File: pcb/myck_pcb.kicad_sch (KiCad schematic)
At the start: 42 parts, among them SW1 SW_Push, SW10 SW_Push, SW11 SW_Push, SW12 SW_Push, SW13 SW_Push, SW14 SW_Push, SW15 SW_Push, SW16 SW_Push, SW17 SW_Push, SW18 SW_Push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

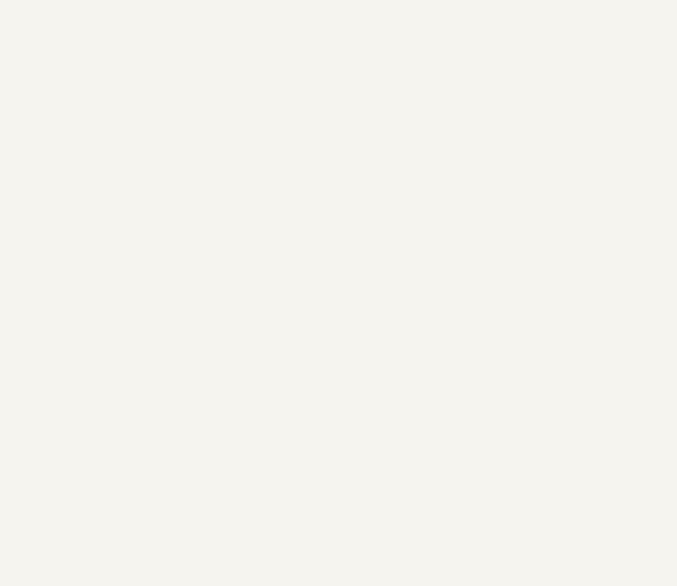
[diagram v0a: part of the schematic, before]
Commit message: Añadidos footprints propios y empezando la PCB
Añadidos footprints propios para:
- diodos
- switches
- microcontrolador
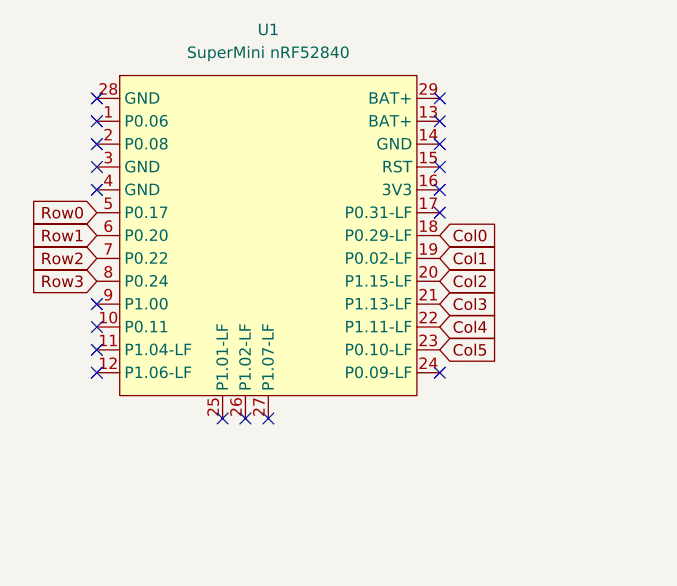
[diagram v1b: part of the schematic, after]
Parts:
- added U1: SuperMini nRF52840, myck:SuperMini_nRF52840_AH_USBup, symbol PCM_marbastlib-promicroish:SuperMini_nRF52840
- D1, D10, D11, D12, D13, D14, D15, D16, D17, D18, D19, D2, D20, D21, D3, D4, D5, D6, D7, D8, D9: footprint (none) -> myck:Diode_TH_SMD_DUAL
- SW1, SW10, SW11, SW12, SW13, SW14, SW15, SW16, SW17, SW18, SW19, SW2, SW20, SW21, SW3, SW4, SW5, SW6, SW7, SW8, SW9: footprint (none) -> myck:KS-27_KS-33_Hotswap_1U_DUAL
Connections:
- net Col0: now also U1.18 (P0.29-LF)
- net Col1: now also U1.19 (P0.02-LF)
- net Col2: now also U1.20 (P1.15-LF)
- net Col3: now also U1.21 (P1.13-LF)
- net Col4: now also U1.22 (P1.11-LF)
- net Col5: now also U1.23 (P0.10-LF)
- net Row0: now also U1.5 (P0.17)
- net Row1: now also U1.6 (P0.20)
- net Row2: now also U1.7 (P0.22)
- net Row3: now also U1.8 (P0.24)
- no-connect marks 0 -> 19

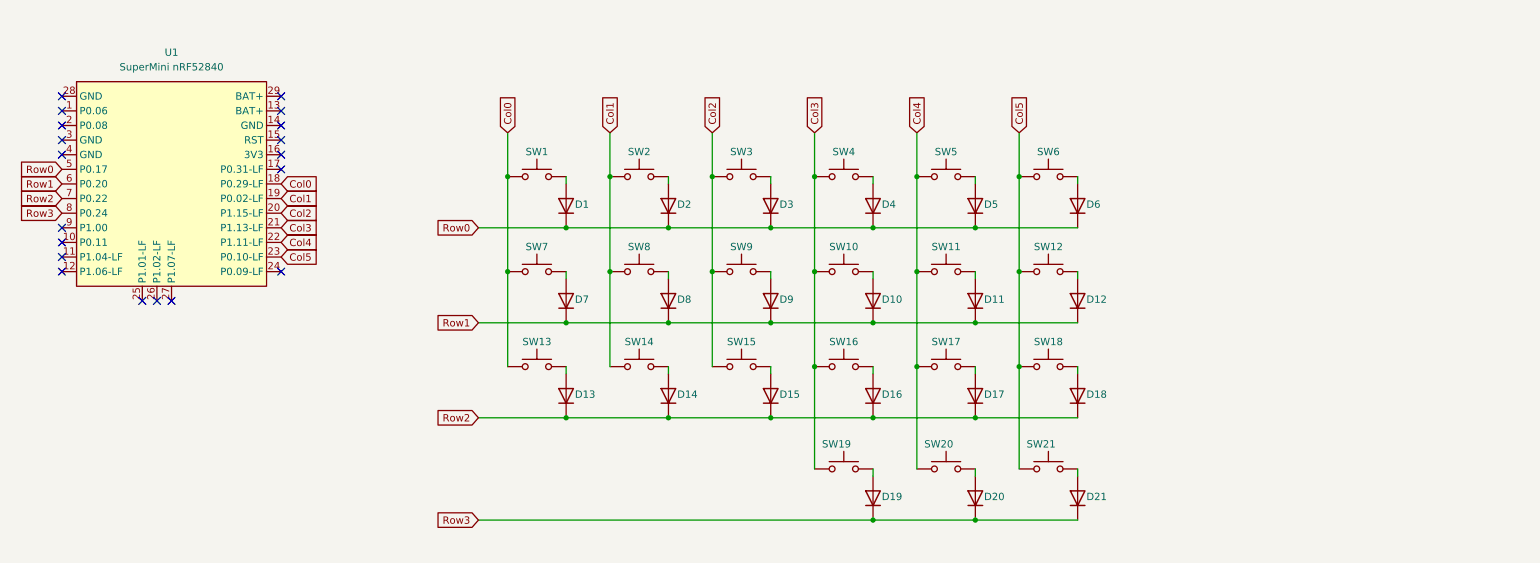
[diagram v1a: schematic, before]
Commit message: Añadidos nice!view reversible
Añadida la opción de tener un nice!view en modo reversible (para ello
se han añadido varios jumpers que tienen que ser soldados antes).
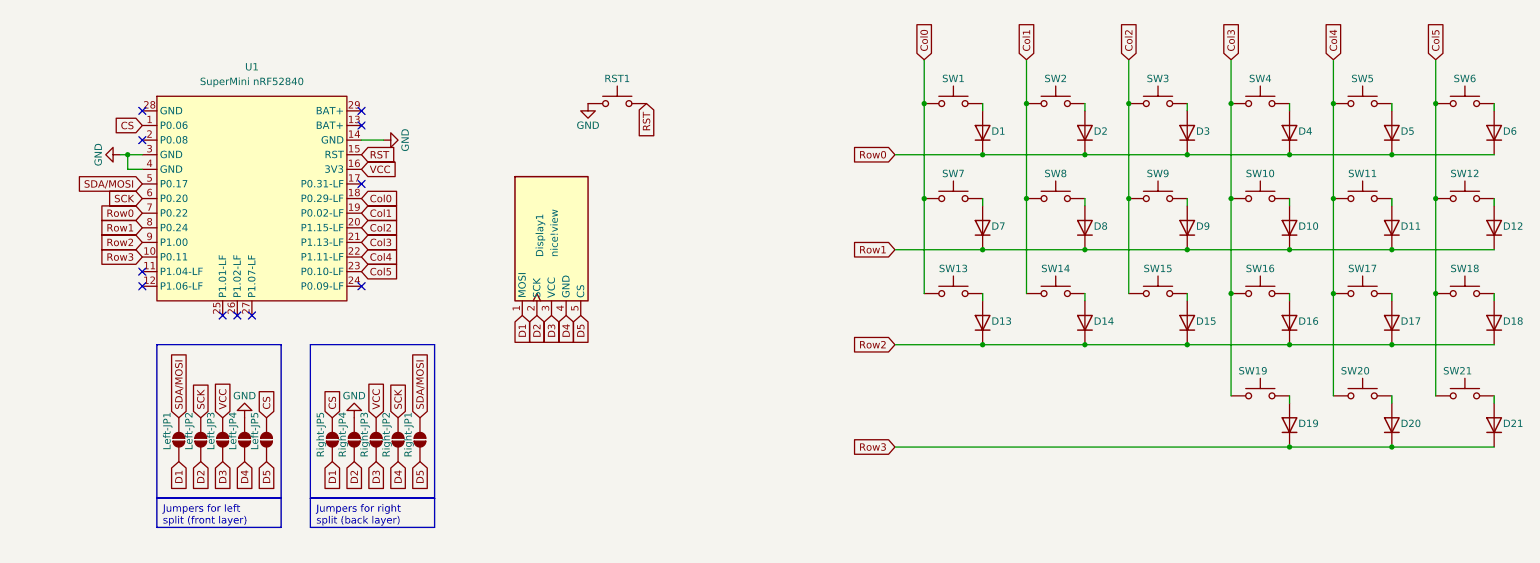
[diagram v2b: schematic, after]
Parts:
- added Display1: nice!view, myck:nice_view, symbol myck:nice!view
- added Left-JP1, Left-JP2, Left-JP3, Left-JP4, Left-JP5, Right-JP1, Right-JP2, Right-JP3, Right-JP4, Right-JP5: SolderJumper_2_Open, Jumper:SolderJumper-2_P1.3mm_Open_TrianglePad1.0x1.5mm, symbol Jumper:SolderJumper_2_Open
- added RST1: SW_Push, symbol Switch:SW_Push
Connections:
- net Row0: now also U1.7 (P0.22); no longer U1.5 (P0.17)
- net Row1: now also U1.8 (P0.24); no longer U1.6 (P0.20)
- net Row2: now also U1.9 (P1.00); no longer U1.7 (P0.22)
- net Row3: now also U1.10 (P0.11); no longer U1.8 (P0.24)
- net CS: now reaches U1.1 (P0.06)
- net CS: now also Left-JP5.2 (B), Right-JP5.2 (B)
- net GND: now reaches U1.14 (GND)
- net GND: now also U1.3 (GND), U1.4 (GND), Left-JP4.2 (B), RST1.1, Right-JP4.2 (B)
- net RST: now reaches U1.15 (RST)
- net RST: now also RST1.2
- net VCC: now reaches U1.16 (3V3)
- net VCC: now also Left-JP3.2 (B), Right-JP3.2 (B)
- new net D1: Display1.1 (MOSI), Left-JP1.1 (A), Right-JP5.1 (A)
- new net D2: Display1.2 (SCK), Left-JP2.1 (A), Right-JP4.1 (A)
- new net D3: Display1.3 (VCC), Left-JP3.1 (A), Right-JP3.1 (A)
- new net D4: Display1.4 (GND), Left-JP4.1 (A), Right-JP2.1 (A)
- new net D5: Display1.5 (CS), Left-JP5.1 (A), Right-JP1.1 (A)
- new net SCK: Left-JP2.2 (B), Right-JP2.2 (B), U1.6 (P0.20)
- new net SDA/MOSI: Left-JP1.2 (B), Right-JP1.2 (B), U1.5 (P0.17)
- no-connect marks 19 -> 11
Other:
- moved on the sheet: D1, D10, D11, D12, D13, D14, D15, D16, D17, D18, D19, D2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

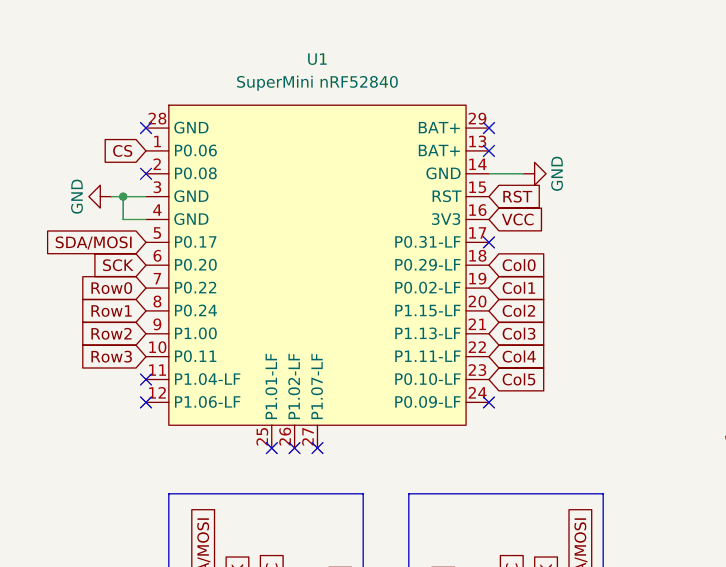
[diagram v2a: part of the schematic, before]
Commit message: Cableado de los diodos terminado
Pequeña modificación en el tamaño de la placa para ignorar errores.
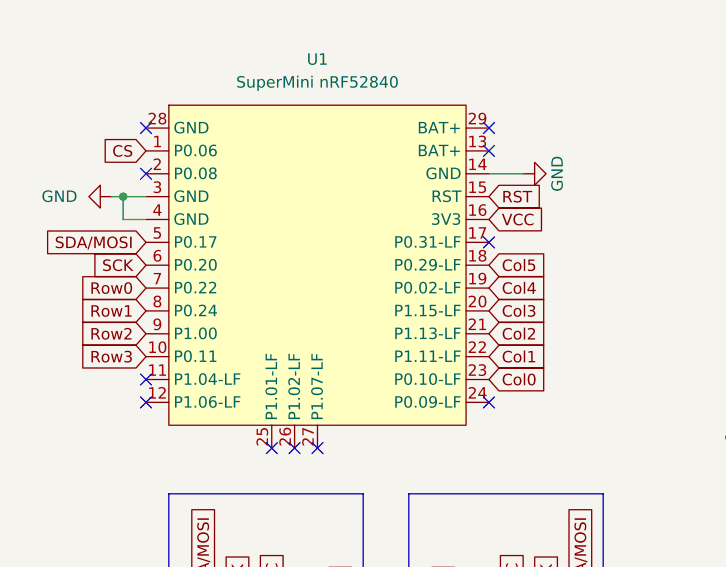
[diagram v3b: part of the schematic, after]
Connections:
- net Col0: now also U1.23 (P0.10-LF); no longer U1.18 (P0.29-LF)
- net Col1: now also U1.22 (P1.11-LF); no longer U1.19 (P0.02-LF)
- net Col2: now also U1.21 (P1.13-LF); no longer U1.20 (P1.15-LF)
- net Col3: now also U1.20 (P1.15-LF); no longer U1.21 (P1.13-LF)
- net Col4: now also U1.19 (P0.02-LF); no longer U1.22 (P1.11-LF)
- net Col5: now also U1.18 (P0.29-LF); no longer U1.23 (P0.10-LF)

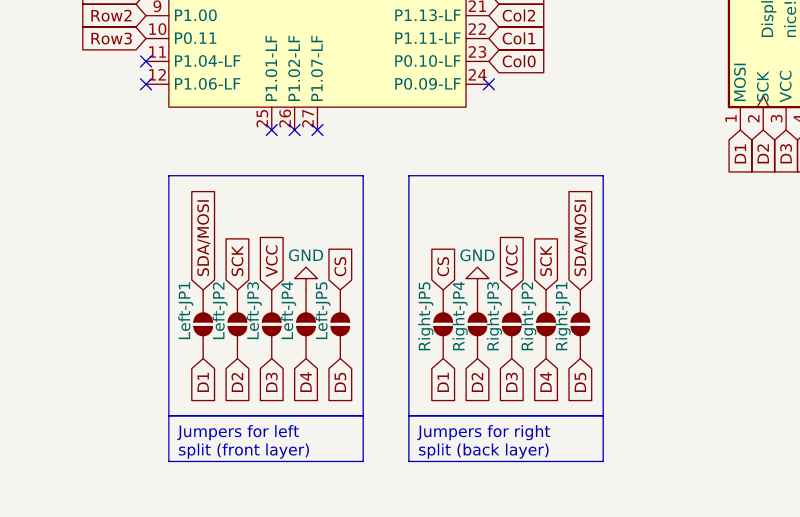
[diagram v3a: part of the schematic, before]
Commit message: Cambios en los jumpers del display
Ahora los jumpers se tienen que soldar en la parte trasera de cada lado (tiene más sentido, todas las soldaduras en la parte de atrás de cada lado).

Añadido una vía de GND para rellenar más zona.
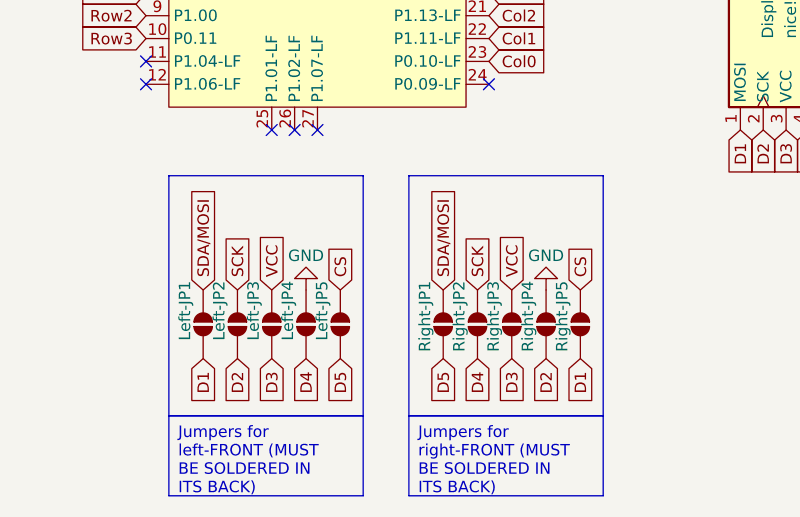
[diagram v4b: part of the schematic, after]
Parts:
- renumbered Right-JP5 to Right-JP1, Right-JP4 to Right-JP2, Right-JP2 to Right-JP4, Right-JP1 to Right-JP5
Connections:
- net CS: now also Right-JP5.2 (B); no longer Right-JP1.2 (B)
- net D1: now also Right-JP5.1 (A); no longer Right-JP1.1 (A)
- net D2: now also Right-JP4.1 (A); no longer Right-JP2.1 (A)
- net D4: now also Right-JP2.1 (A); no longer Right-JP4.1 (A)
- net D5: now also Right-JP1.1 (A); no longer Right-JP5.1 (A)
- net GND: now also Right-JP4.2 (B); no longer Right-JP2.2 (B)
- net SCK: now also Right-JP2.2 (B); no longer Right-JP4.2 (B)
- net SDA/MOSI: now also Right-JP1.2 (B); no longer Right-JP5.2 (B)
